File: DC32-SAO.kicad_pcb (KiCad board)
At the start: 2 copper layers, 50.4 x 50.4 mm, 11 parts, among them J1 Conn_01x06_Male

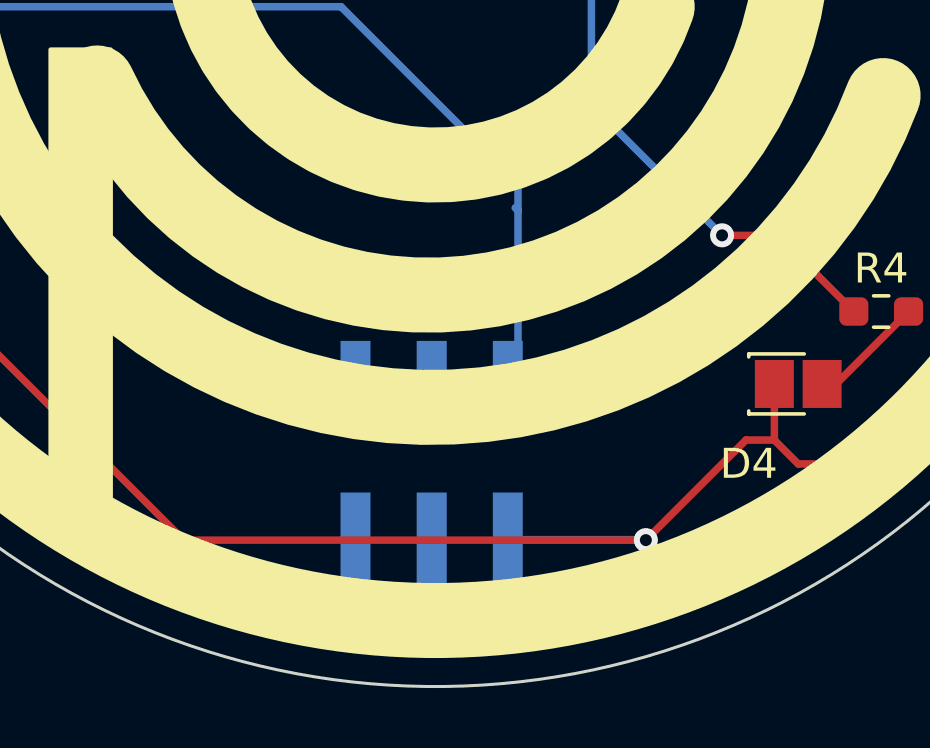
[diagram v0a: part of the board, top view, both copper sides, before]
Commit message: Changed orientation of power pins.
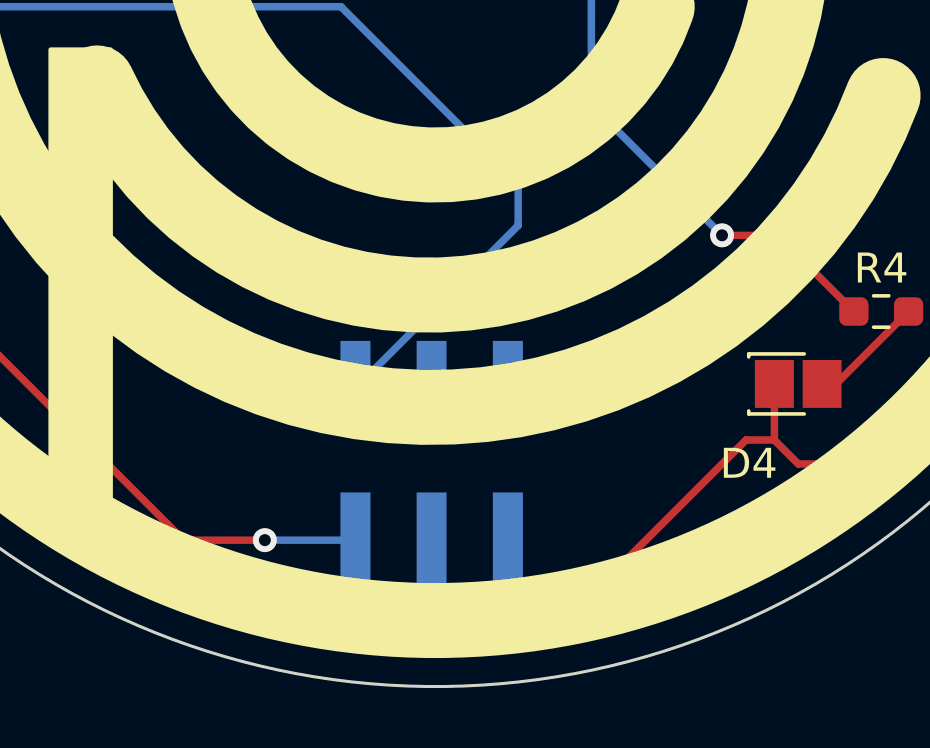
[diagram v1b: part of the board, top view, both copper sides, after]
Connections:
- D1 pad 1: Net-(J1-Pad6) -> Net-(D1-Pad1)
- D2 pad 1: Net-(J1-Pad6) -> Net-(D1-Pad1)
- D3 pad 1: Net-(J1-Pad6) -> Net-(D1-Pad1)
- D4 pad 1: Net-(J1-Pad6) -> Net-(D1-Pad1)
- D5 pad 1: Net-(J1-Pad6) -> Net-(D1-Pad1)
- J1 pad 1: unconnected-(J1-Pad1) -> Net-(J1-Pad1)
- J1 pad 2: unconnected-(J1-Pad2) -> Net-(D1-Pad1)
- J1 pad 5: Net-(R5-Pad1) -> unconnected-(J1-Pad5)
- J1 pad 6: Net-(J1-Pad6) -> unconnected-(J1-Pad6)
- R1 pad 1: Net-(R5-Pad1) -> Net-(J1-Pad1)
- R2 pad 1: Net-(R5-Pad1) -> Net-(J1-Pad1)
- R3 pad 1: Net-(R5-Pad1) -> Net-(J1-Pad1)
- R4 pad 1: Net-(R5-Pad1) -> Net-(J1-Pad1)
- R5 pad 1: Net-(R5-Pad1) -> Net-(J1-Pad1)
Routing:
- net Net-(D1-Pad1): track 0.00 -> 153.6 mm, vias 0 -> 1
- net Net-(J1-Pad6): track 150.7 -> 0.00 mm, vias 1 -> 0
- net Net-(J1-Pad1): track 0.00 -> 99.8 mm, vias 0 -> 3
- net Net-(R5-Pad1): track 97.7 -> 0.00 mm, vias 3 -> 0
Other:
- board text added: "DC32 SAO Board v0.2"
- board text removed: "DC32 SAO Board v0.1"

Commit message: Minting v0.2
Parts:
- D1, D2, D3, D4, D5: footprint LEDs:LED_0606_HandSoldering -> LEDs:LED_0606
- R1, R2, R3, R4, R5: footprint Resistor_SMD:R_0603_1608Metric_Pad0.98x0.95mm_HandSolder -> Resistor_SMD:R_0603_1608Metric
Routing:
- net Net-(D1-Pad1): track 153.6 -> 158.6 mm
- net Net-(J1-Pad1): track 99.8 -> 98.8 mm

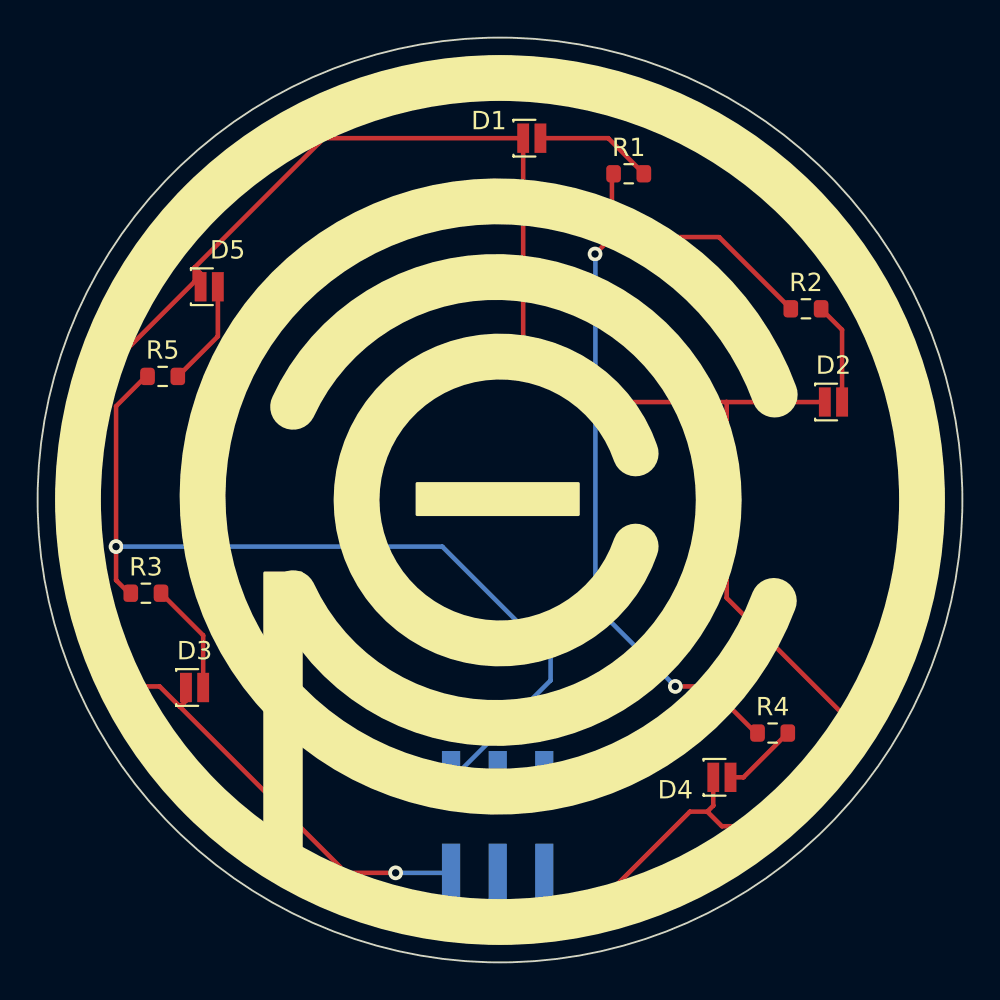
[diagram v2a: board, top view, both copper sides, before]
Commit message: Made through-hole version.
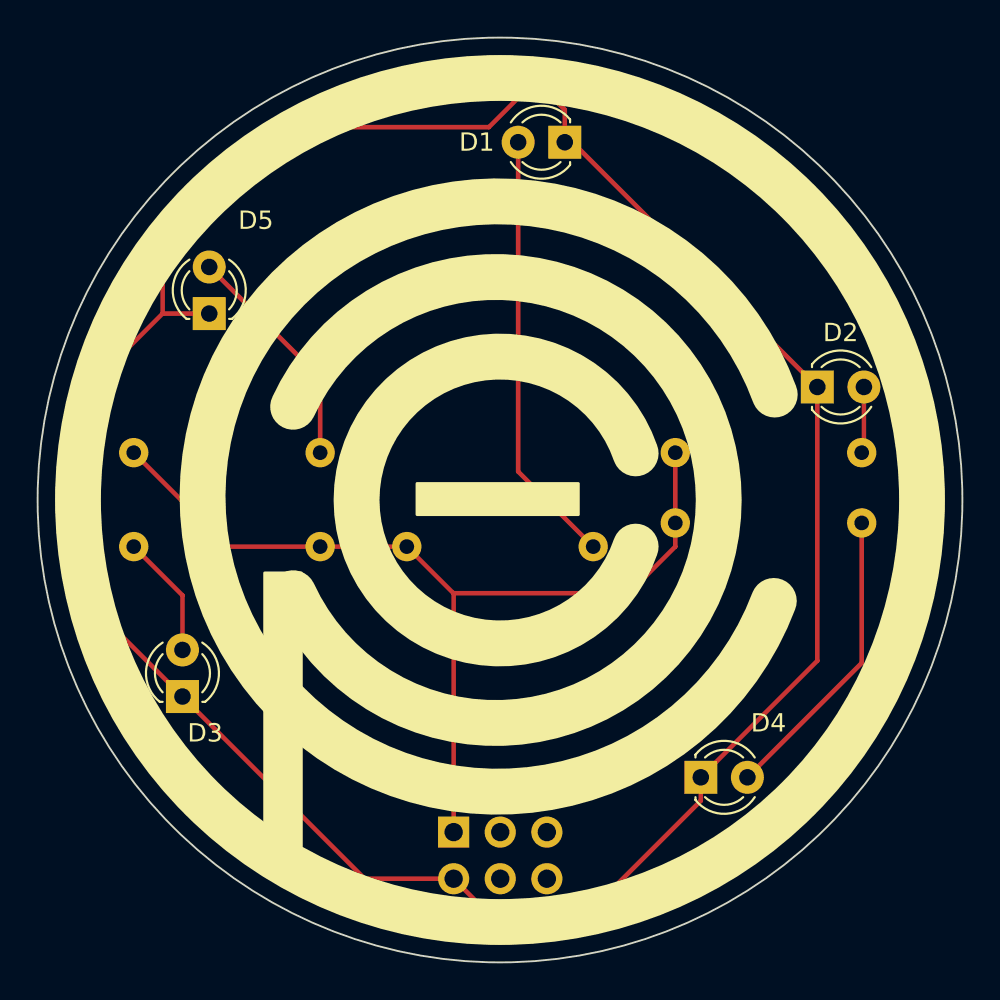
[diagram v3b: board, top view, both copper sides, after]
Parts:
- D1, D2, D3, D4, D5: footprint LEDs:LED_0606 -> LED_THT:LED_D3.0mm
- J1: footprint Connector_PinHeader_2.54mm:PinHeader_2x03_P2.54mm_Vertical_SMD -> Connector_PinHeader_2.54mm:PinHeader_2x03_P2.54mm_Vertical
- R1, R2, R3, R4, R5: value 5 -> 62; footprint Resistor_SMD:R_0603_1608Metric -> Resistor_THT:R_Axial_DIN0207_L6.3mm_D2.5mm_P10.16mm_Horizontal; moved to B.Cu
- moved R1 23.6 mm to (117.4, 78.7)
- moved R4 12.6 mm to (132.1, 77.5)
- moved R2 10.6 mm to (132.1, 73.6)
- moved R3 9.83 mm to (112.7, 78.7), turned to 180 degrees
- moved R5 4.44 mm to (102.6, 73.6)
- moved J1 2.42 mm to (120.0, 94.3)
- moved D1 1.81 mm to (126.1, 56.7), turned to 180 degrees
- moved D5 1.46 mm to (106.7, 66.0), turned to 90 degrees
- moved D2 1.20 mm to (139.8, 70.0)
- moved D4 1.15 mm to (133.5, 91.3)
- moved D3 0.82 mm to (105.2, 86.9), turned to 90 degrees
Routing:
- net Net-(J1-Pad1): track 98.8 -> 51.9 mm, vias 3 -> 0
- net Net-(D1-Pad1): track 158.6 -> 139.6 mm, vias 1 -> 0
- net Net-(D1-Pad2): track 6.44 -> 23.7 mm
- net Net-(D4-Pad2): track 4.12 -> 16.4 mm
- net Net-(D5-Pad2): track 5.79 -> 12.6 mm
- net Net-(D2-Pad2): track 5.55 -> 3.71 mm
- net Net-(D3-Pad2): track 6.09 -> 6.73 mm
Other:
- board text added: "DC32 SAO Board v0.3"
- board text removed: "DC32 SAO Board v0.2"
